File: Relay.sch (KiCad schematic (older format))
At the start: 11 parts, among them K1 1461069-5, Q1 2N3904, U1 LTV-816S

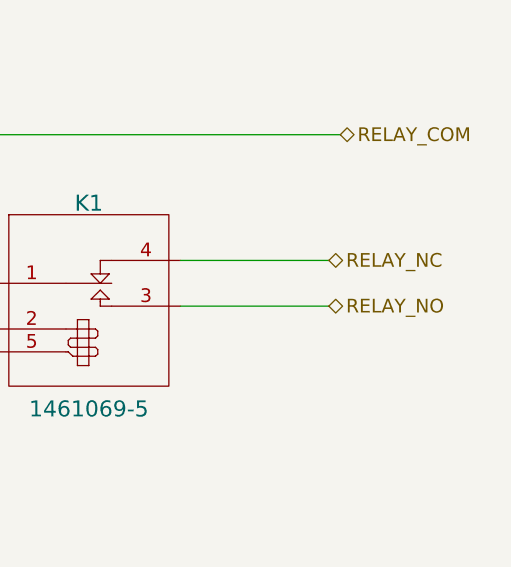
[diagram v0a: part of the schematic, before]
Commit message: Cleanup to schematic after doing a scale printout
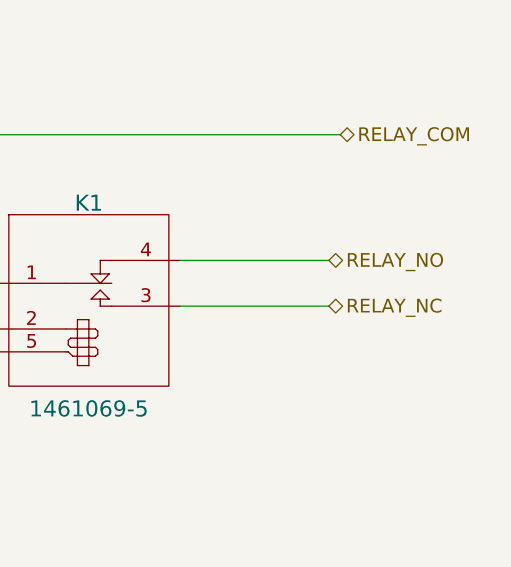
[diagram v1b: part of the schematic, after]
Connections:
- net RELAY_NC: now also K1.3 (NO); no longer K1.4 (NC)
- net RELAY_NO: now also K1.4 (NC); no longer K1.3 (NO)
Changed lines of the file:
@@
-EESchema Schematic File Version 2  date 10/31/2013 9:00:44 PM
+EESchema Schematic File Version 2  date 11/2/2013 7:04:39 PM
 LIBS:power
 LIBS:device
@@
 Sheet 4 9
 Title ""
-Date "1 nov 2013"
+Date "2 nov 2013"
 Rev ""
 Comp ""
@@
 Text HLabel 2300 3750 0    60   Output ~ 0
 RELAY-
+Text HLabel 10450 2850 2    60   BiDi ~ 0
+RELAY_NC
 Text HLabel 10450 2650 2    60   BiDi ~ 0
-RELAY_NC
-Text HLabel 10450 2850 2    60   BiDi ~ 0
 RELAY_NO
 $Comp

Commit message: Layout Work Session 4 Output
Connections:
- net GND renamed GND_RELAY
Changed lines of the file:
@@
-EESchema Schematic File Version 2  date 11/2/2013 7:04:39 PM
+EESchema Schematic File Version 2  date 11/7/2013 10:50:27 PM
 LIBS:power
 LIBS:device
@@
 Sheet 4 9
 Title ""
-Date "2 nov 2013"
+Date "8 nov 2013"
 Rev ""
 Comp ""
@@
 	1    0    0    -1
 $EndComp
-$Comp
-L GND #PWR24
-U 1 1 523B9FB4
-P 8800 5650
-F 0 "#PWR24" H 8800 5650 30  0001 C CNN
-F 1 "GND" H 8800 5580 30  0001 C CNN
-F 2 "" H 8800 5650 60  0000 C CNN
-F 3 "" H 8800 5650 60  0000 C CNN
-	1    8800 5650
-	1    0    0    -1
-$EndComp
 Wire Wire Line
 	8800 5150 8800 5650
@@
 $EndComp
 $Comp
-L +12P #PWR23
+L +12P #PWR020
 U 1 1 523BA00D
 P 6450 1450
-F 0 "#PWR23" H 6450 1420 30  0001 C CNN
+F 0 "#PWR020" H 6450 1420 30  0001 C CNN
 F 1 "+12P" H 6450 1550 30  0000 C CNN
 F 2 "" H 6450 1450 60  0000 C CNN
@@
 	8100 1550 6450 1550
 Connection ~ 6450 1550
+$Comp
+L GND_RELAY #PWR?
+U 1 1 527CF70A
+P 8800 5650
+F 0 "#PWR?" H 8800 5650 30  0001 C CNN
+F 1 "GND_RELAY" H 8800 5580 30  0000 C CNN
+F 2 "~" H 8800 5650 60  0000 C CNN
+F 3 "~" H 8800 5650 60  0000 C CNN
+	1    8800 5650
+	1    0    0    -1
+$EndComp
 $EndSCHEMATC
